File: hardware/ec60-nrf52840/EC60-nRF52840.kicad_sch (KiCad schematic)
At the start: 20 parts, among them J1 REAR_USB_DAUGHTERBOARD, J3 SWD_POGO, SW1 EVQPUC02K_RESET, U1 MDBT50Q-1MV2

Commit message: fix: validate single-nRF PCB and add 3D renders
Complete routing and native clearance repairs, freeze footprint metadata, and preserve EC60 sensing and mounting geometry. Add reproducible KiCad stills and a six-second 3D turntable with model provenance.

Validation: strict DRC 0 errors and 0 opens; ERC 0 errors; 268 physical pin pairs pass with no connectivity regressions. Render source hashes are unchanged, and MP4/GIF decoding passes. Physical assembly and SI/RF validation remain pending.
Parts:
- C13: footprint Capacitor_SMD:C_0402_1005Metric -> YAECKB:C_0402_1005Metric__C13
- C30: footprint Capacitor_SMD:C_0603_1608Metric -> YAECKB:C_0603_1608Metric__C30
- C31: footprint Capacitor_SMD:C_0402_1005Metric -> YAECKB:C_0402_1005Metric__C31
- C32: footprint Capacitor_SMD:C_0603_1608Metric -> YAECKB:C_0603_1608Metric__C32
- D1: footprint Package_TO_SOT_SMD:SOT-143 -> YAECKB:SOT-143__D1
- D2: footprint LED_SMD:LED_0603_1608Metric -> YAECKB:LED_0603_1608Metric__D2
- F1: footprint Fuse:Fuse_1206_3216Metric -> YAECKB:Fuse_1206_3216Metric__F1
- J1: footprint YAECKB:JST-SR-4 -> YAECKB:JST-SR-4__J1
- J3: footprint YAECKB:SWD_Pogo_2x03 -> YAECKB:SWD_Pogo_2x03__J3; now left out of the parts list
- R26: footprint Resistor_SMD:R_0402_1005Metric -> YAECKB:R_0402_1005Metric__R26
- R3: footprint Resistor_SMD:R_0402_1005Metric -> YAECKB:R_0402_1005Metric__R3
- R30: footprint Resistor_SMD:R_0402_1005Metric -> YAECKB:R_0402_1005Metric__R30
- R31: footprint Resistor_SMD:R_0402_1005Metric -> YAECKB:R_0402_1005Metric__R31
- R32: footprint Resistor_SMD:R_0402_1005Metric -> YAECKB:R_0402_1005Metric__R32
- R4: footprint Resistor_SMD:R_0402_1005Metric -> YAECKB:R_0402_1005Metric__R4
- R5: footprint Resistor_SMD:R_0402_1005Metric -> YAECKB:R_0402_1005Metric__R5
- R6: footprint Resistor_SMD:R_0402_1005Metric -> YAECKB:R_0402_1005Metric__R6
- R7: footprint Resistor_SMD:R_0402_1005Metric -> YAECKB:R_0402_1005Metric__R7
- SW1: footprint Button_Switch_SMD:Panasonic_EVQPUL_EVQPUC -> YAECKB:Panasonic_EVQPUL_EVQPUC__SW1
- U1: footprint RF_Module:Raytac_MDBT50Q -> YAECKB:Raytac_MDBT50Q__U1

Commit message: feat: checkpoint YETI60 electrical review and firmware simulation
Replace inherited USB series resistance with 0R links for the nRF52840 PHY. Add a schematic-derived pin contract, portable scan/power/HID control core and ASan/UBSan host simulation. Begin YETI60 branding and English/Chinese documentation migration.

CAD: zero strict DRC errors, zero opens and all 268 physical pin pairs pass. Host simulation passes; real peripherals and transport stacks remain mocked. Power-route optimization, assembly Z fit, battery-space study, assembled renders and remaining bilingual documents continue after this checkpoint.
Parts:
- R30, R31: value 27 -> 0

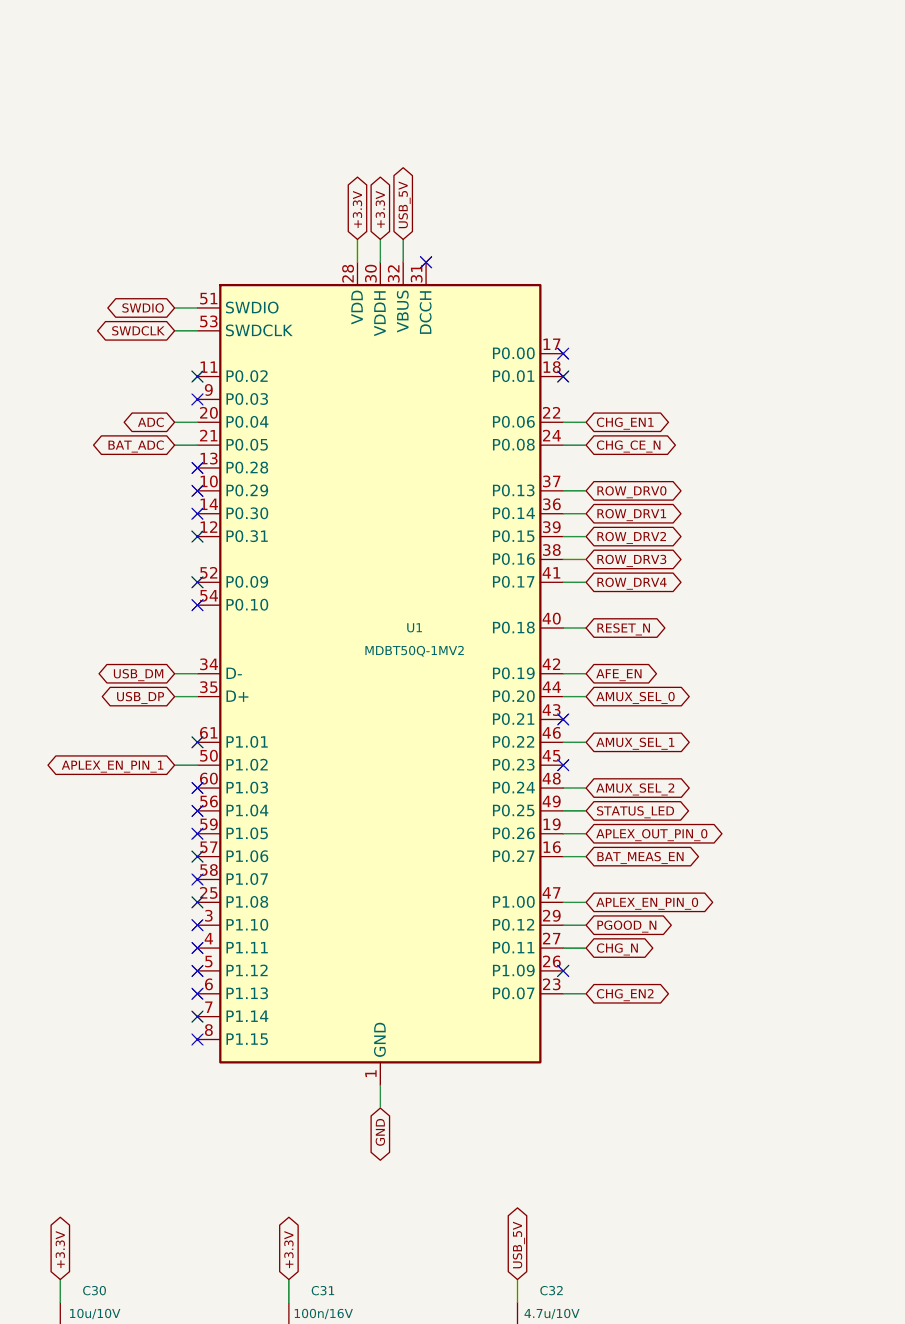
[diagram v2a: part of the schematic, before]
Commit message: feat: implement E73 schematic and buildable USB BLE firmware checkpoint
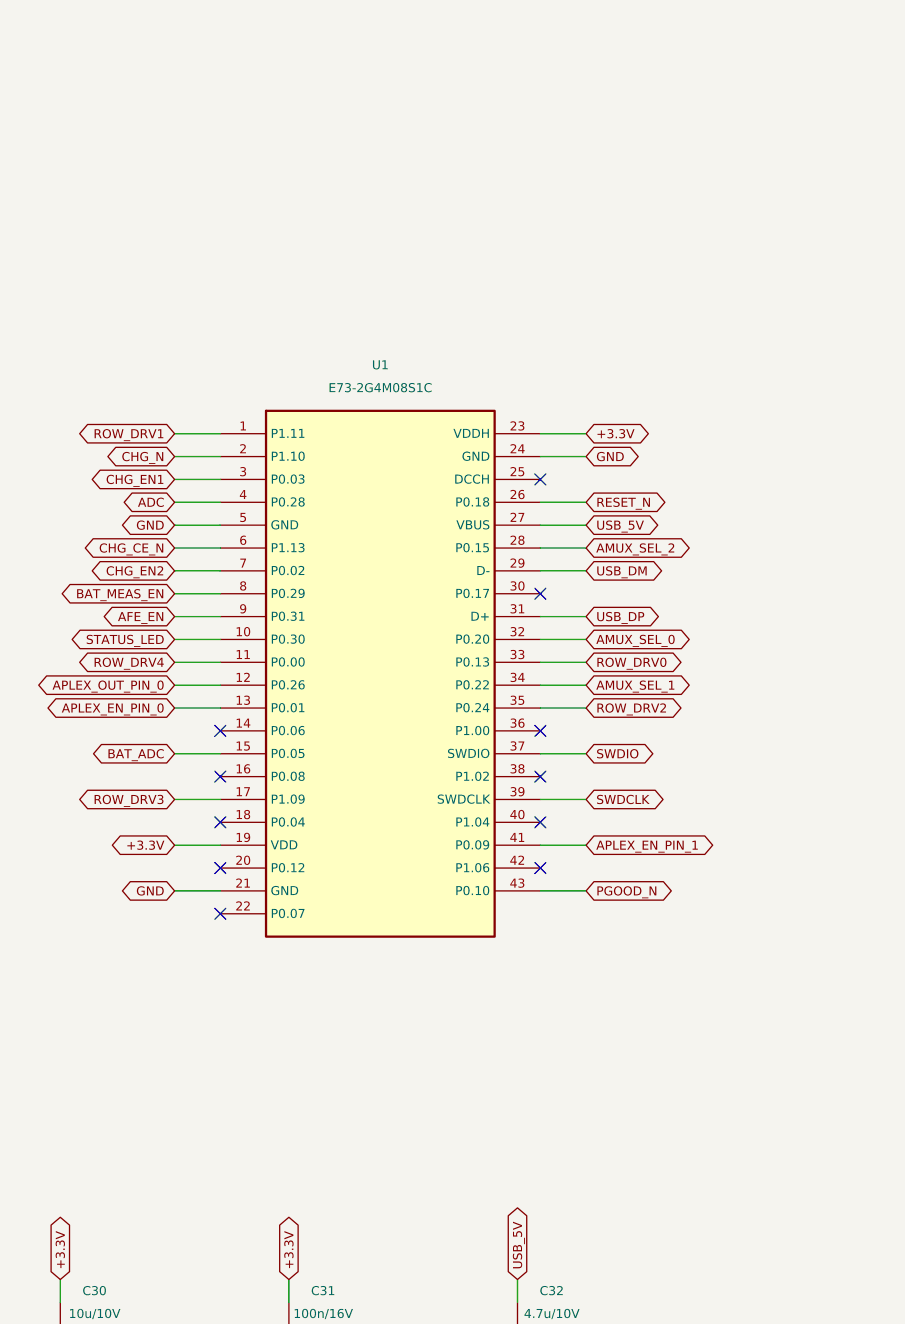
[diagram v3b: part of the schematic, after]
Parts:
- U1: value MDBT50Q-1MV2 -> E73-2G4M08S1C; footprint YAECKB:Raytac_MDBT50Q__U1 -> YAECKB:E73-2G4M08S1C__U1; symbol YAECKB:MDBT50Q-1MV2 -> YAECKB:E73-2G4M08S1C
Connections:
- net +3.3V: now also U1.19 (VDD), U1.23 (VDDH); no longer U1.28 (VDD), U1.30 (VDDH)
- net ADC: now also U1.4 (P0.28); no longer U1.20 (P0.04)
- net AFE_EN: now also U1.9 (P0.31); no longer U1.42 (P0.19)
- net AMUX_SEL_0: now also U1.32 (P0.20); no longer U1.44 (P0.20)
- net AMUX_SEL_1: now also U1.34 (P0.22); no longer U1.46 (P0.22)
- net AMUX_SEL_2: now also U1.28 (P0.15); no longer U1.48 (P0.24)
- net APLEX_EN_PIN_0: now also U1.13 (P0.01); no longer U1.47 (P1.00)
- net APLEX_EN_PIN_1: now also U1.41 (P0.09); no longer U1.50 (P1.02)
- net APLEX_OUT_PIN_0: now also U1.12 (P0.26); no longer U1.19 (P0.26)
- net BAT_ADC: now also U1.15 (P0.05); no longer U1.21 (P0.05)
- net BAT_MEAS_EN: now also U1.8 (P0.29); no longer U1.16 (P0.27)
- net CHG_CE_N: now also U1.6 (P1.13); no longer U1.24 (P0.08)
- net CHG_EN1: now also U1.3 (P0.03); no longer U1.22 (P0.06)
- net CHG_EN2: now also U1.7 (P0.02); no longer U1.23 (P0.07)
- net CHG_N: now also U1.2 (P1.10); no longer U1.27 (P0.11)
- net GND: now also U1.21 (GND), U1.24 (GND), U1.5 (GND); no longer U1.1 (GND), U1.15 (GND), U1.2 (GND), U1.33 (GND), U1.55 (GND)
- net PGOOD_N: now also U1.43 (P0.10); no longer U1.29 (P0.12)
- net RESET_N: now also U1.26 (P0.18); no longer U1.40 (P0.18)
- net ROW_DRV0: now also U1.33 (P0.13); no longer U1.37 (P0.13)
- net ROW_DRV1: now also U1.1 (P1.11); no longer U1.36 (P0.14)
- net ROW_DRV2: now also U1.35 (P0.24); no longer U1.39 (P0.15)
- net ROW_DRV3: now also U1.17 (P1.09); no longer U1.38 (P0.16)
- net ROW_DRV4: now also U1.11 (P0.00); no longer U1.41 (P0.17)
- net STATUS_LED: now also U1.10 (P0.30); no longer U1.49 (P0.25)
- net SWDCLK: now also U1.39 (SWDCLK); no longer U1.53 (SWDCLK)
- net SWDIO: now also U1.37 (SWDIO); no longer U1.51 (SWDIO)
- net USB_5V: now also U1.27 (VBUS); no longer U1.32 (VBUS)
- net USB_DM: now also U1.29 (D-); no longer U1.34 (D-)
- net USB_DP: now also U1.31 (D+); no longer U1.35 (D+)
- no-connect marks 27 -> 11
